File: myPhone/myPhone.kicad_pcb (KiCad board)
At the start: 4 copper layers, 135 x 70 mm, 234 parts, among them J1 USB_OTG, J2 BATT, J202 Modem, J203 SIM_Card, J204 Motor, J205 Micro_SD_Card, J206 Camera, J3 SJ-3571N, J301 iMX8, J302 Touch, J303 Display, J304 Prog, Q1 MMBT3906, SW1 RESET, SW2 WAKE, SW201 BOOT, U1 BQ25895, U10 74HC595, U11 ICS-43434, U12 MAX98357A, U13 FT813Q, U14 FAN5333BSX, U2 TPS62293, U201 ESP32-WROOM, U202 SN74CBTLV3125, U203 TXB0104RGY, U204 TXB0104RGY, U205 DRV2605L, U206 SN74CBTLV3126, U207 TPS22917, U208 SN74LVC2G66, U209 TPS22917, U3 TPS630250, U301 SN65LVDS822_SWAP, U302 TS3DDR3812, U303 TS3DDR3812, U304 TS3DDR3812, U5 E310-G002, U6 IS25LP128-JBLE, U7 74HC00, U8 74HC00, U9 74HC595, X1 SiT1533, Y1 16MHz, Y2 12MHz

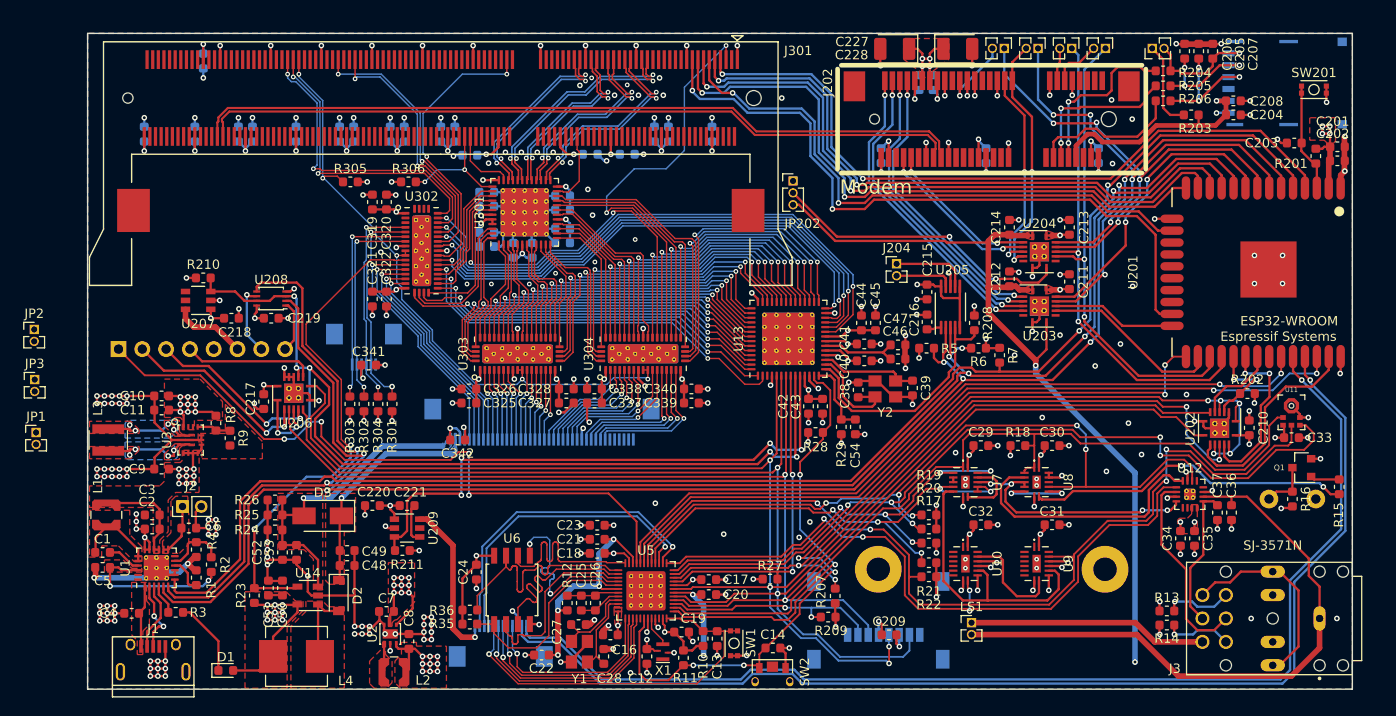
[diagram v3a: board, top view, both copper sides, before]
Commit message: fixed battery charger; added i2c switch for fe310; swapped pwm1/pwm2 for mic/spk
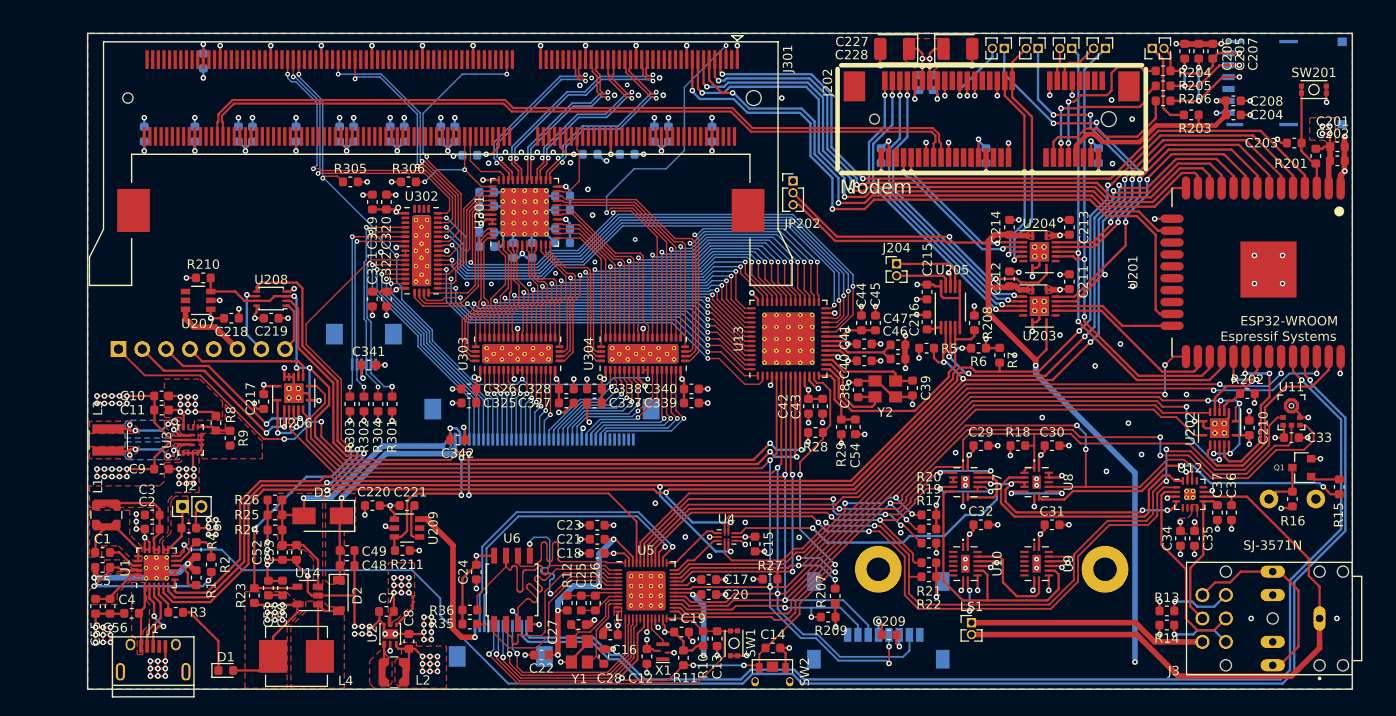
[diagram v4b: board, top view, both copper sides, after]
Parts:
- removed JP1: VSYS, Connector_PinHeader_1.27mm:PinHeader_1x02_P1.27mm_Vertical
- removed JP2: 3V3, Connector_PinHeader_1.27mm:PinHeader_1x02_P1.27mm_Vertical
- removed JP3: 1V8, Connector_PinHeader_1.27mm:PinHeader_1x02_P1.27mm_Vertical
- added C15: 0.1uF, Capacitor_SMD:C_0603_1608Metric, F.Cu at (168.4, 126.3)
- added C55: 22uF, Capacitor_SMD:C_0603_1608Metric, F.Cu at (98.0, 132.9)
- added C56: 22uF, Capacitor_SMD:C_0603_1608Metric, F.Cu at (99.6, 132.9)
- added U4: TMUX154E, Package_DFN_QFN:UQFN-10_1.3x1.8mm_P0.4mm, F.Cu at (165.4, 125.5)
- moved R19 1.50 mm to (187.0, 124.7)
- moved R20 1.50 mm to (187.0, 123.2)
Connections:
- net ESP32.BQ_INT renamed ESP32.IO39
- net ESP32.I2C0.SCL renamed TMUX.I2C0.SCL
- net ESP32.I2C0.SDA renamed TMUX.I2C0.SDA
- R17 pad 2: PWM2.2 -> PWM1.2
- R22 pad 2: GPIO_20 -> /I2S_SD_OUT
- U1 pad 12: Net-(U1-Pad12) -> WAKE
- U10 pad 9: GPIO_13 -> /I2S_SD_IN
- U11 pad 1: PWM2.1 -> PWM1.1
- U11 pad 6: GPIO_20 -> /I2S_SD_OUT
- U12 pad 1: GPIO_13 -> /I2S_SD_IN
- U12 pad 14: PWM1.1 -> PWM2.1
- U201 pad 36: GPIO_21 -> GPIO_20
- U5 pad 36: PWM2.2 -> GPIO_12
- U5 pad 43: GPIO_21 -> PWM1.2
- U7 pad 13: PWM2.2 -> PWM1.2
- U7 pad 2: PWM2.2 -> PWM1.2
- U8 pad 10: PWM1.1 -> PWM2.1
- U9 pad 14: GPIO_20 -> /I2S_SD_OUT
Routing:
- net /I2S_SD_OUT: track 0.00 -> 90.1 mm, vias 0 -> 4
- net GPIO_21: track 83.4 -> 0.00 mm, vias 2 -> 0
- net /I2S_SD_IN: track 0.00 -> 68.0 mm, vias 0 -> 4
- net GPIO_13: track 74.8 -> 7.02 mm, vias 4 -> 0
- net WAKE: track 90.8 -> 149.7 mm, vias 6 -> 8
- net PWM1.2: track 0.00 -> 52.9 mm, vias 0 -> 5
- net PWM2.2: track 47.6 -> 0.00 mm, vias 5 -> 0
- net /SPK_EN: track 27.2 -> 59.6 mm, vias 4 -> 5
- net GPIO_20: track 99.8 -> 82.9 mm, vias 4 -> 2
- net TMUX.I2C0.SDA: track 186.6 -> 198.8 mm, vias 7 -> 9
- net TMUX.I2C0.SCL: track 185.6 -> 195.4 mm, vias 6 -> 8
- net PWM2.1: track 87.3 -> 78.8 mm
- net PWM1.1: track 82.3 -> 90.4 mm
- net GND: track 419.9 -> 426.6 mm, vias 286 -> 290
- net GPIO_12: track 0.00 -> 6.08 mm
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- added copper zone on F.Cu, net Net-(C55-Pad1)

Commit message: solder mask clearance/width fixed; REV1 board
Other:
- rule pad_to_mask_clearance: 0.03 -> 0.045
- rule solder_mask_min_width: 0.13 -> 0.11
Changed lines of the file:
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@@
     (pad_size 0.9 0.95)
     (pad_drill 0)
-    (pad_to_mask_clearance 0.03)
-    (solder_mask_min_width 0.13)
+    (pad_to_mask_clearance 0.045)
+    (solder_mask_min_width 0.11)
     (aux_axis_origin 97.2 71.8)
     (visible_elements FFFFFFFF)
